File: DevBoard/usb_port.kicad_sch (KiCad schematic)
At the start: 127 parts, among them J401 TYPE-C 16PCB0.8 IP68, J402 I2CC logic analyzer, Q401 IAUC45N04S6L063H, Q402 IAUC45N04S6L063H, Q403 AO3401A, Q404 AO3401A, Q405 AO3400A, Q406 AO3400A, U401 TPS25751DREFR, U402 M24512-DFMC6TG, U403 BQ25756RRVR, U404 TPS62933DRLR, U405 TPD2S300YFFR

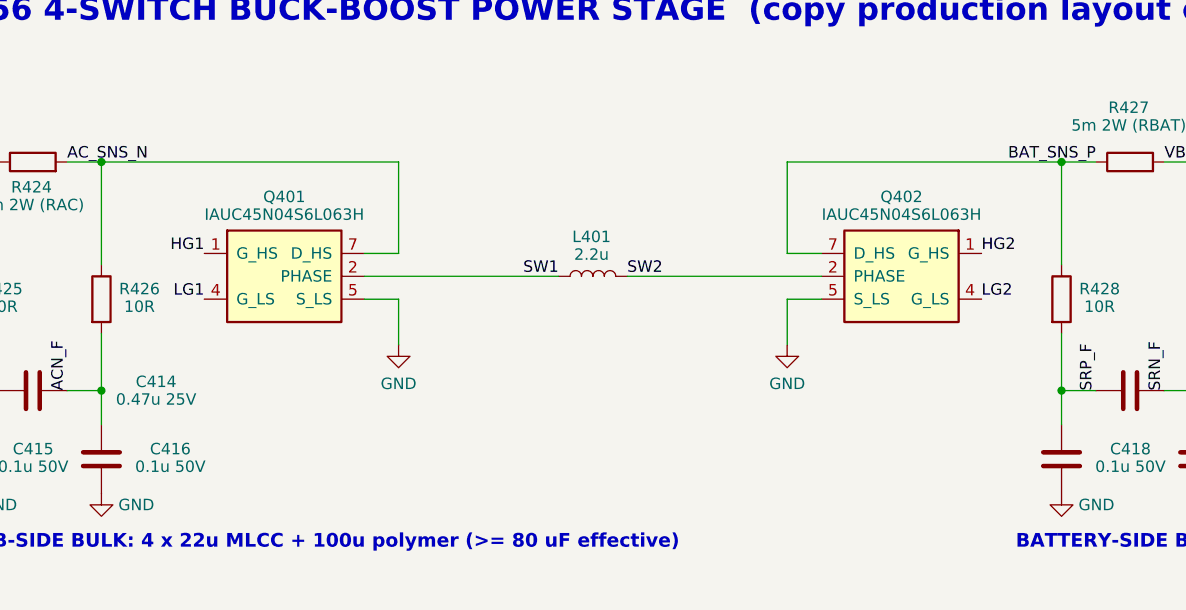
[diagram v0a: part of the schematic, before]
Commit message: Dev board: charger half-bridges -> discrete PGQ04N070 FETs
Each IAUC45N04S6L063H half-bridge ($1.16, 62 at JLC) becomes two JinYu
PGQ04N070 (C49384056, $0.12, PDFN3333 on the AGM PDFN3.3x3.3 footprint):
Q401/Q407 USB side, Q402/Q408 battery side, and the 5xx twins. 40 V,
10 mOhm max at 4.5 V (IAUC45: 8.5), Qg 14.7 nC; matches the production
plan of discrete 3.3 x 3.3 mm FETs. New PGQ04N070 symbol, power stage
redrawn, docs and costed BOM updated: about $77 per board at 5 boards.

Co-Authored-By: Claude Opus 5.5 <noreply@anthropic.com>
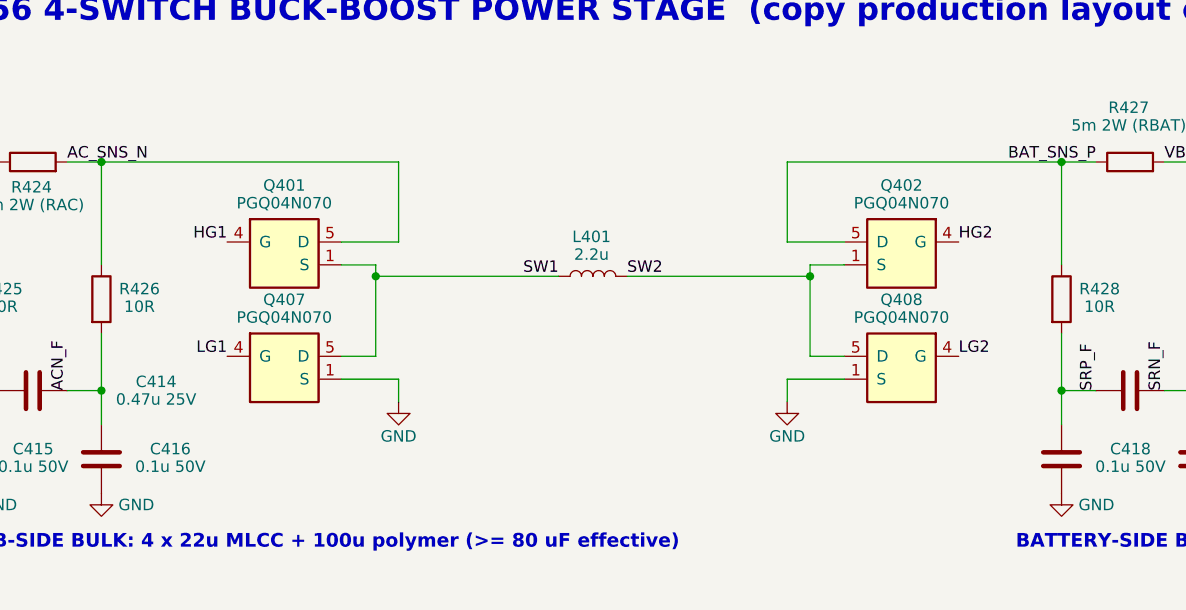
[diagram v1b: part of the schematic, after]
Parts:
- removed Q401, Q402: IAUC45N04S6L063H, MonolithDev:Infineon_PG-TDSON-8-57_HalfBridge, symbol MonolithDev:IAUC45N04S6L063H
- added Q401, Q402, Q407, Q408: PGQ04N070, MonolithDev:AGM_PDFN-8_3.3x3.3mm_P0.65mm, symbol MonolithDev:PGQ04N070
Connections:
- net AC_SNS_N: now also Q401.5 (D), Q401.6 (D), Q401.7 (D), Q401.8 (D)
- net BAT_SNS_P: now also Q402.5 (D), Q402.6 (D), Q402.7 (D), Q402.8 (D)
- net GND: now also Q407.1 (S), Q407.2 (S), Q407.3 (S), Q408.1 (S), Q408.2 (S), Q408.3 (S)
- net HG1: now also Q401.4 (G)
- net HG2: now also Q402.4 (G)
- net LG1: now also Q407.4 (G)
- net LG2: now also Q408.4 (G)
- net SW1: now also Q401.1 (S), Q401.2 (S), Q401.3 (S), Q407.5 (D), Q407.6 (D), Q407.7 (D), Q407.8 (D)
- net SW2: now also Q402.1 (S), Q402.2 (S), Q402.3 (S), Q408.5 (D), Q408.6 (D), Q408.7 (D), Q408.8 (D)

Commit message: Dev board: 6-layer 1.6 mm board, TPD4S201 port protector, 1.6 mm USB-C
- Stack-up: 6 layers, 1.6 mm, 2 oz outer / 0.5 oz inner (In1/In4 GND),
  0.3 mm drill / 0.45 mm via minimum so JLC's small-via surcharge is gone.
  Via-in-pad (POFV) is free on 6+ layers.
- U405/U505: TPD2S300 (0.4 mm DSBGA) -> TPD4S201TRGRRQ1 (VQFN-20 RGR),
  CC + SBU protection with FLT -> GPIO3. D402/D502 and C453/C553 removed.
- J401/J501: Shou Han TYPE-C 16PCB1.6 IP68 (C55629729), footprint and
  STEP model generated for the 1.6 mm board.
- TPS25751 REF0038A thermal vias 0.2 -> 0.3 mm.
- setup_board.py keeps unmanaged net classes (Kelvin); reset_board.py
  reloads swapped footprints in place.
- ERC 0 errors, DRC schematic parity 0. BOM $77.17 -> $78.65 per board
  at 5 boards.

Co-Authored-By: Claude Opus 5.5 <noreply@anthropic.com>
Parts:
- removed C453: 1u 50V, Capacitor_SMD:C_0603_1608Metric, symbol Device:C
- removed D402: ESD2CAN24DBZRQ1, Package_TO_SOT_SMD:SOT-23, symbol MonolithDev:ESD2CAN24
- removed U405: TPD2S300YFFR, MonolithDev:TI_YFF0009_DSBGA-9_P0.4mm, symbol MonolithDev:TPD2S300
- added U405: TPD4S201TRGRRQ1, MonolithDev:TI_RGR0020C_VQFN-20-1EP_3.5x3.5mm_P0.5mm_EP2.05mm, symbol MonolithDev:TPD4S201
- C451: Notes TPD2S300 VBIAS (ESD support): 0.1 uF, >= 35 V rated (50 V r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 -> TPD4S201 VBIAS (ESD support): 0.1 uF, 50 V (C_CC/C_SBU can 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
- C452: Notes TPD2S300 VPWR decoupling (0.3-1 uF recommended) -> TPD4S201 VPWR decoupling (EVM C68: 1 uF)
- J401: value TYPE-C 16PCB0.8 IP68 -> TYPE-C 16PCB1.6 IP68; footprint MonolithDev:USB_C_Receptacle_ShouHan_TYPE-C_16PCB0.8_IP68 -> MonolithDev:USB_C_Receptacle_ShouHan_TYPE-C_16PCB1.6_IP68; LCSC C55629727 -> C55629729; MPN TYPE-C 16PCB0.8 IP68 -> TYPE-C 16PCB1.6 IP68 (Shou Han)
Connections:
- net CC1: now also U405.12 (CC1); no longer J401.A5 (CC1)
- net CC2: now also U405.11 (CC2); no longer J401.B5 (CC2)
- net GND: now also U405.13 (GND), U405.18 (GND), U405.21 (GND), U405.8 (GND)
- net LDO_3V3: now also U405.10 (VPWR)
- net SBU1: now also U405.1 (C_SBU1)
- net SBU1_SNS: now also U405.15 (SBU1)
- net SBU2: now also U405.2 (C_SBU2)
- net SBU2_SNS: now also U405.14 (SBU2)
- net SBU_FLT: now also U405.9 (~{FLT})
- net at C451.1: now also U405.3 (VBIAS)
- new net: U405.16 (NC), U405.17 (NC), U405.19 (NC), U405.20 (NC)
- new net C_CC1: J401.A5 (CC1), U405.4 (C_CC1), U405.7 (RPD_G1)
- new net C_CC2: J401.B5 (CC2), U405.5 (C_CC2), U405.6 (RPD_G2)
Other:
- note added: "NOTES (this sheet is used twice: USB Port 1 = 4xx, USB Port 2 = 5xx) 1. Address straps are on the root sheet: port 1 ADCIN1 = LDO_3V3, ADCIN2 = GND (0x20); port 2 ADCIN1 = ADCIN2 = GND (0x21). Both are SafeMode (TPS25751 table 8-6). 2. Unused TPS25751 GPIOs (0, 1, 2, 11) tied to GND per datasheet (KiCad ERC flags this; expected). Never configure them as outputs. 3. CC and SBU are protected by U40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"
- note removed: "NOTES (this sheet is used twice: USB Port 1 = 4xx, USB Port 2 = 5xx) 1. Address straps are on the root sheet: port 1 ADCIN1 = LDO_3V3, ADCIN2 = GND (0x20); port 2 ADCIN1 = ADCIN2 = GND (0x21). Both are SafeMode (TPS25751 table 8-6). 2. Unused TPS25751 GPIOs (0, 1, 2, 11) tied to GND per datasheet (KiCad ERC flags this; expected). Never configure them as outputs. 3. At the connector pins: D402 CC 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"
- moved on the sheet: R441

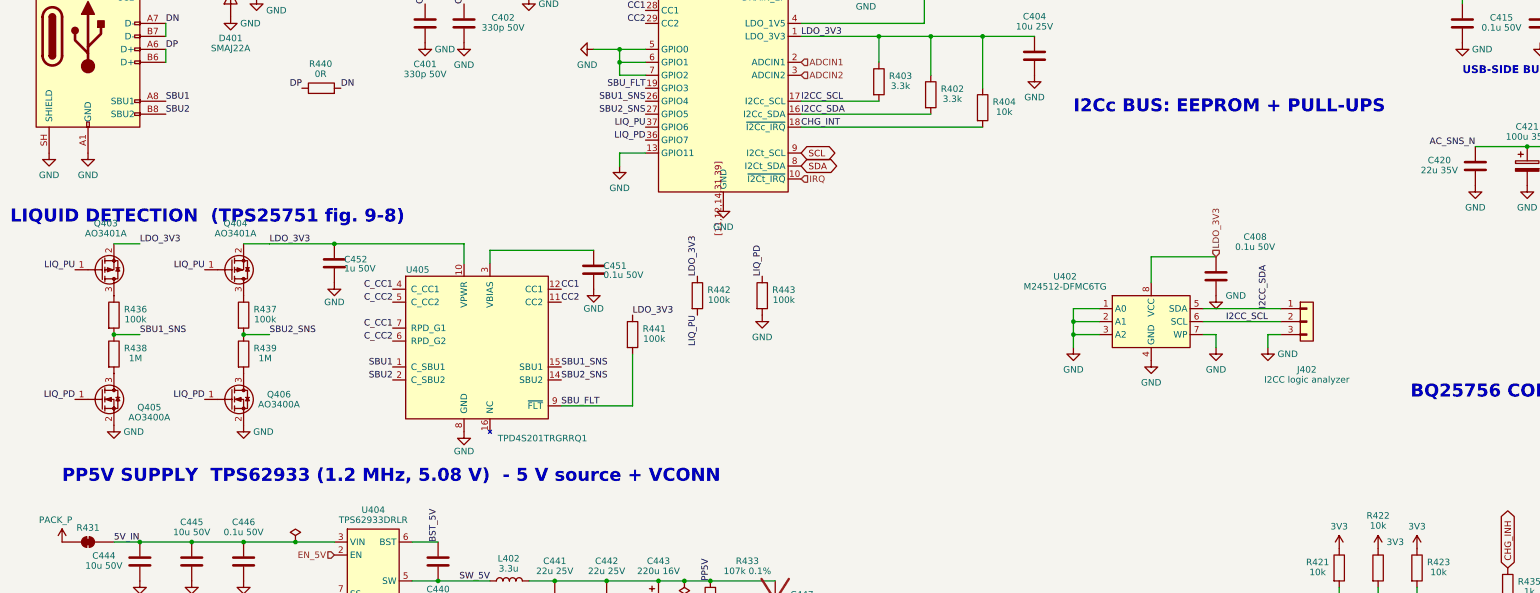
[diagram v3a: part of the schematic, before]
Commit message: Dev board schematic: tidy pass
- Title blocks on every sheet: rev A6, 2026-10-14, status line updated
  (was "Not reviewed, laid out, built or tested"); tidy_fields.py
  writes the same.
- Port sheet: the TPD4S201 block is titled with liquid detection
  ("CC/SBU PROTECTION (TPD4S201) + LIQUID DETECTION") and moved clear of
  the heading it collided with; I2Cc heading moved next to the EEPROM;
  PP5V heading clear of U405's GND.
- MCU sheet: test-point row out of the title block, with a heading;
  long NOTES lines wrapped inside the page border.
- Gauge sheet: cell-stack heading clear of its note; TP106 joins the
  test-point row.
- Top sheet: sheet index updated (BQ294700, TPD4S201, TH1-TH5) and
  spaced from the strap note and revision log; rev log line for the
  placement and this tidy.
- New tools/move_region.py moves a rectangle of a sheet (symbols,
  fields, wires, labels) by an offset.

Netlist identical before and after (265 nets); ERC 0 errors;
check_overlaps TOTAL 0.

Co-Authored-By: Claude Opus 5.5 <noreply@anthropic.com>
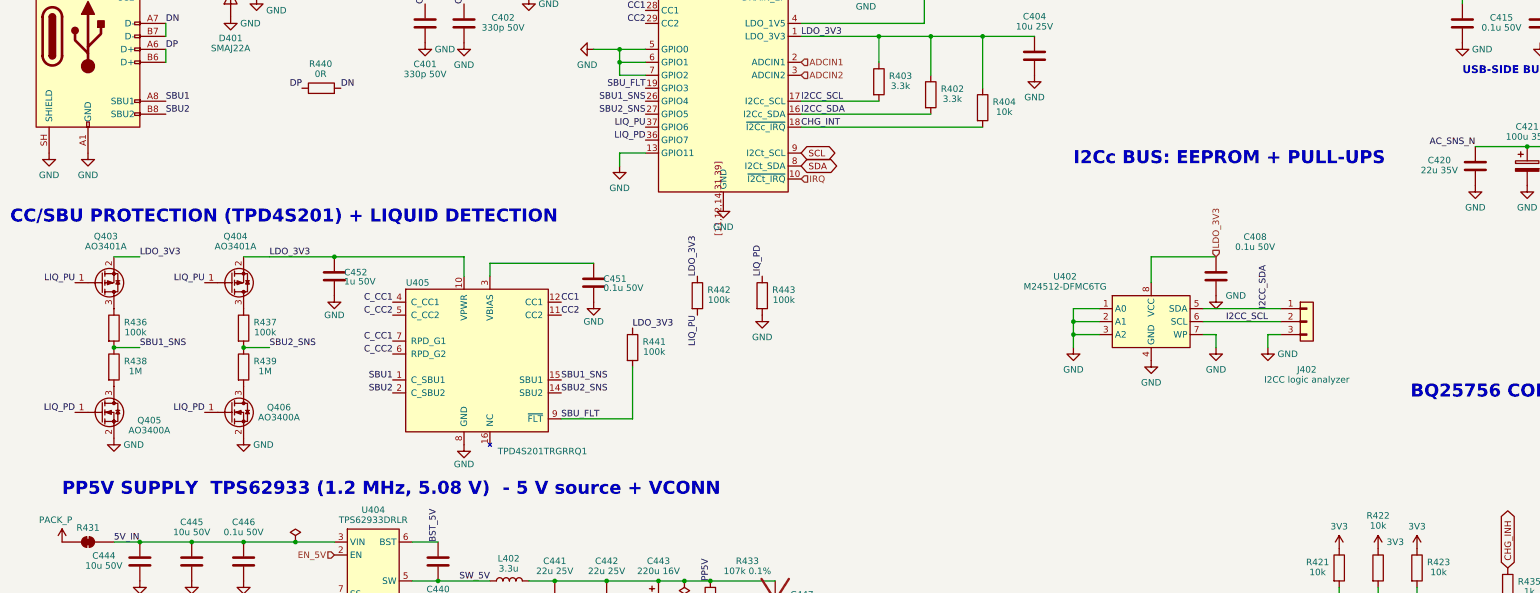
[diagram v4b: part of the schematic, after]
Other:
- note added: "CC/SBU PROTECTION (TPD4S201) + LIQUID DETECTION"
- note removed: "LIQUID DETECTION (TPS25751 fig. 9-8)"
- moved on the sheet: C451, C452, Q403, Q404, Q405, Q406, R436, R437, R438, R439, R441, U405

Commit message: Dev board rev A8: review 4 pre-routing hardware fixes
Applied by tools/review4_fixes.py (one-shot from the rev A7 sheets);
part numbers checked against JLC's parts API.
- R313 470k -> 220k (3V3_SLEEP margin), R314 100k -> 47k (IRQ_N),
  R304/R305 4.7k -> 3.3k (I2C rise time)
- R322/R323 1k in series with J302 TX/RX; R324 1k at J303 pin 2
- C314 placeholder 1p C0G (DNP); C401/C402 330p -> 220p (CC capacitance)
- R450/R451 snubber resistors -> 1206 0.66 W (a 2010/0612 doesn't fit)
- D401/D501 SMAJ22A -> TVS2200DRVR flat clamp (stock KiCad symbol and
  footprint; datasheet added)
- TP415-TP421 (+5xx) 1 mm probe pads on CC, SBU and liquid-detect nets
Board synced and placed (place_blocks.py): 428 parts, 0 parity issues,
no courtyard overlaps. ERC: the 8 known warnings. README item 41,
schematic PDF and placement PNG regenerated.

Co-Authored-By: Claude Opus 5.5 <noreply@anthropic.com>
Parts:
- removed D401: SMAJ22A, Diode_SMD:D_SMA, symbol Device:D_Zener
- added D401: TVS2200DRVR, Package_SON:WSON-6-1EP_2x2mm_P0.65mm_EP1x1.6mm, symbol Power_Protection:TVS2200DRV
- added TP415: CC1, TestPoint:TestPoint_Pad_D1.0mm, symbol Connector:TestPoint
- added TP416: CC2, TestPoint:TestPoint_Pad_D1.0mm, symbol Connector:TestPoint
- added TP417: SBU_FLT, TestPoint:TestPoint_Pad_D1.0mm, symbol Connector:TestPoint
- added TP418: SBU1_SNS, TestPoint:TestPoint_Pad_D1.0mm, symbol Connector:TestPoint
- added TP419: SBU2_SNS, TestPoint:TestPoint_Pad_D1.0mm, symbol Connector:TestPoint
- added TP420: LIQ_PU, TestPoint:TestPoint_Pad_D1.0mm, symbol Connector:TestPoint
- added TP421: LIQ_PD, TestPoint:TestPoint_Pad_D1.0mm, symbol Connector:TestPoint
- C401, C402: value 330p 50V -> 220p 50V; LCSC C13533 -> C307445; MPN CL05C331JB5NNNC -> CL05C221JB5NNNC; Notes 50V C0G -> 50V C0G. 220 pF: with the TPD4S201's 40-120 pF the CC total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
- R450: footprint Resistor_SMD:R_0805_2012Metric -> Resistor_SMD:R_1206_3216Metric; LCSC C16257 -> C3998398; MPN 0805W8F330KT5E -> ERJ-P08J3R3V; Notes DNP RC snubber on SW1 (EVM R14/R15 placeholder). Size R and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 -> DNP RC snubber on SW1 (EVM R14/R15 placeholder). 1206 anti-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
- R451: footprint Resistor_SMD:R_0805_2012Metric -> Resistor_SMD:R_1206_3216Metric; LCSC C16257 -> C3998398; MPN 0805W8F330KT5E -> ERJ-P08J3R3V; Notes DNP RC snubber on SW2 (EVM R14/R15 placeholder). Size R and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 -> DNP RC snubber on SW2 (EVM R14/R15 placeholder). 1206 anti-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
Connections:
- net CC1: now also TP415.1
- net CC2: now also TP416.1
- net GND: now also D401.1 (GND), D401.2 (GND), D401.3 (GND), D401.7 (GND)
- net LIQ_PD: now also TP421.1
- net LIQ_PU: now also TP420.1
- net SBU1_SNS: now also TP418.1
- net SBU2_SNS: now also TP419.1
- net SBU_FLT: now also TP417.1
- net VBUS: now also D401.4 (IN), D401.5 (IN), D401.6 (IN)

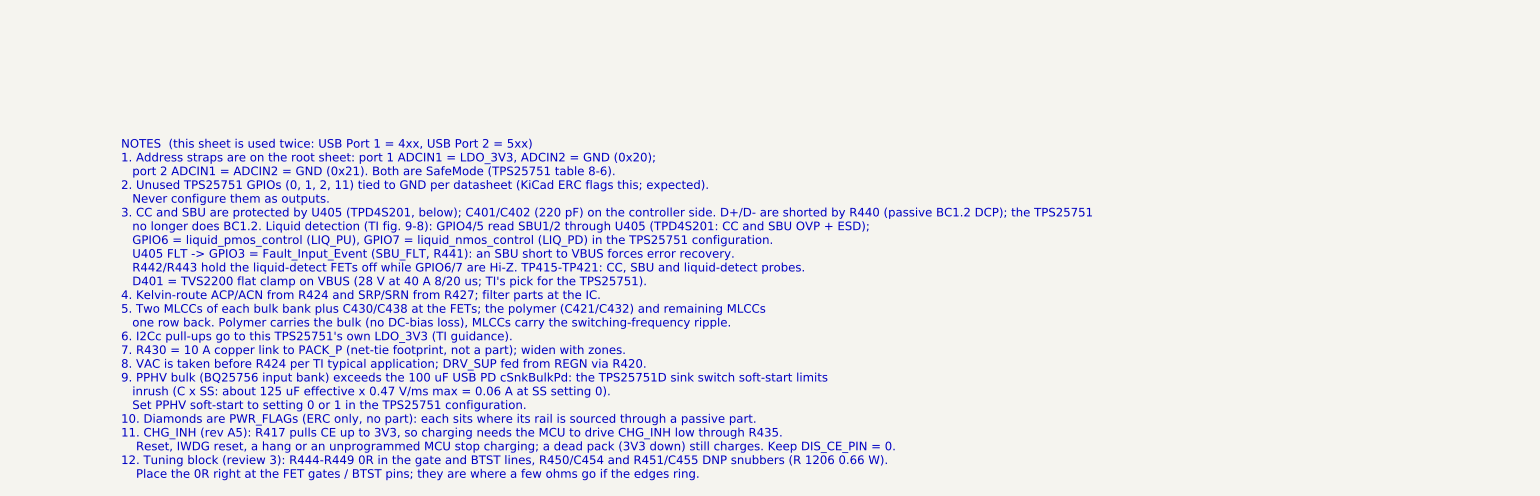
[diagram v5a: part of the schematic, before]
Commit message: Dev board rev A8 part 2: review 4 docs, BOM, A-2 procedure, J104 clamp
Schematic edits by tools/review4_docs.py (helpers split out of
review4_fixes.py into tools/sch_edit.py; review4_fixes output unchanged).
- A-2: EV2400 work only with 3V3 up (J104) and U301 in reset; checklist,
  R312/R301 Notes and MCU sheet note 10 rewritten.
- D-5: D105 SMAJ18A clamp on the J104 side of D104; board placed
  (D104 moved one body width left).
- Stale Notes, sheet notes, heading and address text fixed; sheet 4
  renamed "MCU and Sensors"; revision log A7/A8; title blocks A8.
- MPNs filled on the parts that had only LCSC numbers; Sourcing on U301
  and J301; J301 out of the position file.
- bringup-config-checklist, mcu-io-power-states and power-budget rewritten
  for the CC2340 with every review 4 CONFIG item; corrections in
  circuit-description, cost-down and cc2340-pin-budget.
ERC: 8 known warnings. 0 text overlaps. DRC: 0 parity issues, no
courtyard overlaps (429 parts). README item 42.

Co-Authored-By: Claude Opus 5.5 <noreply@anthropic.com>
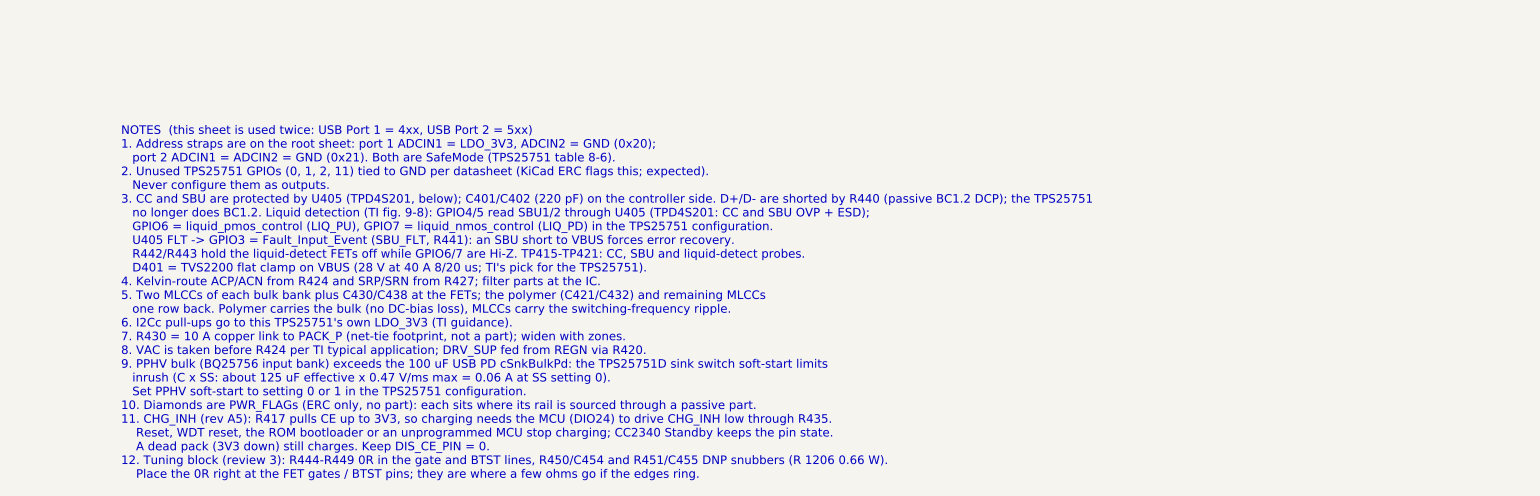
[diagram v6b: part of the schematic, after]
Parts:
- C403, C404: MPN (none) -> CL21A106KAYNNNE
- C405: MPN (none) -> CL10A106KP8NNNC
- C431, C434, C435: Notes Battery-side ripple MLCC (cost-down 2026-10-14, was 47 uF 1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 -> Battery-side ripple MLCC (C431/C434/C435 and C531/C534/C535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
- C451: Notes TPD4S201 VBIAS (ESD support): 0.1 uF, 50 V (C_CC/C_SBU can 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 -> TPD4S201 VBIAS (ESD support), 0.1 uF 50 V X7R. The part's o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
- L401: Notes Cost-down 2026-10-14 (was Coilcraft XAL7030-222, $9.43): 2.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 -> Cost-down 2026-10-14 (was Coilcraft XAL7030-222): 2.2 uH, D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
- L402: Notes Cost-down 2026-10-14 (was SRP5030T-3R3M): 3.3 uH, 38 mOhm max, Irms 5 A, Isat 8 A (review 2: > 5.8 A IHS limit) -> Cost-down 2026-10-14 (was SRP5030T-3R3M): 3.3 uH, 38 mOhm max, Irms 5 A, Isat 8 A defined at a 40 % drop (not like-for-like with the SRP5030T); fine, as the 5.8 A IHS limit is a fault-only peak
- R417: Notes CE pull-up to 3V3: charging is inhibited unless the MCU drives CHG_INH low (reset, hang, unprogrammed or Standby all inhibit). With 3V3 down (dead pack) CE reads low, so USB can still revive the pack. MCU low through R435: CE = 3.3 x 1k/48k = 0.07 V (VIL max 0.4 V) -> CE pull-up to 3V3: charging is inhibited unless the MCU drives CHG_INH (DIO24) low. Reset, WDT reset, ROM bootloader or an unprogrammed MCU all inhibit (pins float). CC2340 Standby keeps the GPIO state, so a low CHG_INH keeps charging in Standby. With 3V3 down (dead pack) CE reads low, so USB can still revive the pack. MCU low through R435/R535: CE = 3.3 x 1k/48k = 0.07 V (VIL max 0.4 V)
- R418: MPN (none) -> RT0805BRD07100KL
- R419: MPN (none) -> RT0805BRD0710KL
- R434: MPN (none) -> RT0805BRD0720KL
- R435: Notes CHG_INH from the MCU (PB8): low allows charging; high or hi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 -> CHG_INH from the MCU (DIO24): low allows charging; high or 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
- R441: Notes TPD2S300 FLT pull-up (open drain, 1.7-300k to 2.7-5.5 V). F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 -> TPD4S201 FLT pull-up (open drain; 1.7-300 kOhm to 2.7-5.5 V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
- R444: Notes HIDRV1 -> Q401 high-side gate (EVM R8). 0R; raise to a few 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 -> HIDRV1 -> Q401/Q501 high-side gate (EVM R8). 0R; raise to a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
- R445: Notes LODRV1 -> Q401 low-side gate (EVM R20). 0R; raise to a few 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 -> LODRV1 -> Q407/Q507 low-side gate (EVM R20). 0R; raise to a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
- R446: Notes HIDRV2 -> Q402 high-side gate (EVM R3). 0R; raise to a few 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 -> HIDRV2 -> Q402/Q502 high-side gate (EVM R3). 0R; raise to a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
- R447: Notes LODRV2 -> Q402 low-side gate (EVM R17). 0R; raise to a few 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 -> LODRV2 -> Q408/Q508 low-side gate (EVM R17). 0R; raise to a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
- R448: Notes BTST1 pin -> C412/D404 (EVM R13). 0R; raise to a few ohms t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 -> BTST1 pin -> C412/D404 (C512/D504) (EVM R13). 0R; raise to 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
- R449: Notes BTST2 pin -> C413/D405 (EVM R23). 0R; raise to a few ohms t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 -> BTST2 pin -> C413/D405 (C513/D505) (EVM R23). 0R; raise to 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
- U401: MPN (none) -> TPS25751DREFR
- U402: MPN (none) -> M24512-DFMC6TG
- U403: MPN (none) -> BQ25756RRVR
- U404: MPN (none) -> TPS62933DRLR
